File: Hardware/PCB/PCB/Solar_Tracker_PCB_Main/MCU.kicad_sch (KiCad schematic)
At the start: 1 part, among them IC1 ESP32-S3-WROOM-1-N4R8

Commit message: actualizacion de pcb
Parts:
- added C13: 22u, symbol Device:C
- added C16, C18, C19: 0.1u, symbol Device:C
- added C17: 1u, symbol Device:C
- added R16: 0, symbol Device:R
- added R2: 10k, symbol Device:R
- added SW1, SW3: ~, symbol Switch:SW_MEC_5G
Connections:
- net GND: now reaches IC1.1 (GND_1)
- net GND: now also IC1.40 (GND_2), IC1.41 (GND_3), IC1.42 (GND_4), IC1.43 (GND_5), IC1.44 (GND_6), IC1.45 (GND_7), IC1.46 (GND_8), IC1.47 (GND_9), IC1.48 (GND_10), IC1.49 (GND_11), C13.2, C16.2, C17.2, C18.2, C19.2, SW1.1 (A), SW1.2 (A), SW3.1 (A), SW3.2 (A)
- net VDD: now reaches IC1.2 (3V3)
- net VDD: now also C13.1, C16.1, R2.1
- net BOOT: now reaches IC1.27 (IO0)
- net BOOT: now also C19.1, SW3.3 (B), SW3.4 (B)
- net EN: now reaches IC1.3 (EN)
- net EN: now also C17.1, R16.2, R2.2
- new net: C18.1, R16.1, SW1.3 (B), SW1.4 (B)
- no-connect marks 0 -> 35
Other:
- moved on the sheet: IC1

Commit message: actualizacion pcb principal
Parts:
- removed R16: 0, symbol Device:R
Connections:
- net EN: now also C18.1, SW1.3 (B), SW1.4 (B)
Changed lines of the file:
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@@
-	(wire
-		(pts
-			(xy 96.52 22.86) (xy 97.79 22.86)
-		)
-		(stroke
-			(width 0)
-			(type default)
-		)
-	)
 	(wire
 		(pts
@@
 	(wire
 		(pts
-			(xy 86.36 22.86) (xy 88.9 22.86)
+			(xy 86.36 22.86) (xy 97.79 22.86)
 		)
 		(stroke
@@
 		(pts
 			(xy 71.12 22.86) (xy 71.12 29.21)
+		)
+		(stroke
+			(width 0)
+			(type default)
+		)
+	)
+	(wire
+		(pts
+			(xy 30.48 34.29) (xy 30.48 33.02)
 		)
 		(stroke
@@
 	(symbol
 		(lib_id "power:GND")
-		(at 30.48 33.02 0)
+		(at 30.48 34.29 0)
 		(unit 1)
 		(exclude_from_sim no)
@@
 		(fields_autoplaced yes)
 		(property "Reference" "#PWR042"
+			(at 30.48 40.64 0)
+			(effects
+				(font
+					(size 1.27 1.27)
+				)
+				(hide yes)
+			)
+		)
+		(property "Value" "GND"
 			(at 30.48 39.37 0)
 			(effects
@@
 					(size 1.27 1.27)
 				)
-				(hide yes)
-			)
-		)
-		(property "Value" "GND"
-			(at 30.48 38.1 0)
-			(effects
-				(font
-					(size 1.27 1.27)
-				)
 			)
 		)
 		(property "Footprint" ""
-			(at 30.48 33.02 0)
+			(at 30.48 34.29 0)
 			(effects
 				(font
@@
 		)
 		(property "Datasheet" ""
-			(at 30.48 33.02 0)
+			(at 30.48 34.29 0)
 			(effects
 				(font
@@
 		)
 		(property "Description" "Power symbol creates a global label with name \"GND\" , ground"
-			(at 30.48 33.02 0)
+			(at 30.48 34.29 0)
 			(effects
 				(font
@@
 					(unit 1)
 				)
-			)
-		)
-	)
-	(symbol
-		(lib_id "Device:R")
-		(at 92.71 22.86 90)
-		(unit 1)
-		(exclude_from_sim no)
-		(in_bom yes)
-		(on_board yes)
-		(dnp no)
-		(property "Reference" "R16"
-			(at 92.71 18.796 90)
-			(effects
-				(font
-					(size 1.27 1.27)
-				)
-			)
-		)
-		(property "Value" "0"
-			(at 92.71 20.574 90)
-			(effects
-				(font
-					(size 1.27 1.27)
-				)
-			)
-		)
-		(property "Footprint" ""
-			(at 92.71 24.638 90)
-			(effects
-				(font
-					(size 1.27 1.27)
-				)
-				(hide yes)
-			)
-		)
-		(property "Datasheet" "~"
-			(at 92.71 22.86 0)
-			(effects
-				(font
-					(size 1.27 1.27)
-				)
-				(hide yes)
-			)
-		)
-		(property "Description" "Resistor"
-			(at 92.71 22.86 0)
-			(effects
-				(font
-					(size 1.27 1.27)
-				)
-				(hide yes)
-			)
-		)
-		(pin "2"
-		)
-		(pin "1"
-		)
-		(instances
-			(project "Solar_Tracker_PCB_Main"
-				(path "/99b6ddd9-7ffe-4c85-972a-e0f594a166d4/521ed49f-67a8-4f65-9cb7-064f532bae28"
-					(reference "R16")
-					(unit 1)
-				)

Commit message: Actualizacion de Footprints Resistencias y Capacitores Main PCB
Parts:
- C13, C16, C17, C18, C19: footprint (none) -> Capacitor_SMD:C_0805_2012Metric_Pad1.18x1.45mm_HandSolder
- R2: footprint (none) -> Resistor_SMD:R_0805_2012Metric_Pad1.20x1.40mm_HandSolder
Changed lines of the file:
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@@
 			)
 		)
-		(property "Footprint" ""
+		(property "Footprint" "Capacitor_SMD:C_0805_2012Metric_Pad1.18x1.45mm_HandSolder"
 			(at 117.8052 35.56 0)
 			(effects
@@
 			)
 		)
-		(property "Footprint" ""
+		(property "Footprint" "Resistor_SMD:R_0805_2012Metric_Pad1.20x1.40mm_HandSolder"
 			(at 54.61 29.718 90)
 			(effects
@@
 			)
 		)
-		(property "Footprint" ""
+		(property "Footprint" "Capacitor_SMD:C_0805_2012Metric_Pad1.18x1.45mm_HandSolder"
 			(at 50.8 33.9852 0)
 			(effects
@@
 			)
 		)
-		(property "Footprint" ""
+		(property "Footprint" "Capacitor_SMD:C_0805_2012Metric_Pad1.18x1.45mm_HandSolder"
 			(at 74.93 30.1752 0)
 			(effects
@@
 			)
 		)
-		(property "Footprint" ""
+		(property "Footprint" "Capacitor_SMD:C_0805_2012Metric_Pad1.18x1.45mm_HandSolder"
 			(at 21.2852 33.02 0)
 			(effects
@@
 			)
 		)
-		(property "Footprint" ""
+		(property "Footprint" "Capacitor_SMD:C_0805_2012Metric_Pad1.18x1.45mm_HandSolder"
 			(at 31.4452 33.02 0)
 			(effects

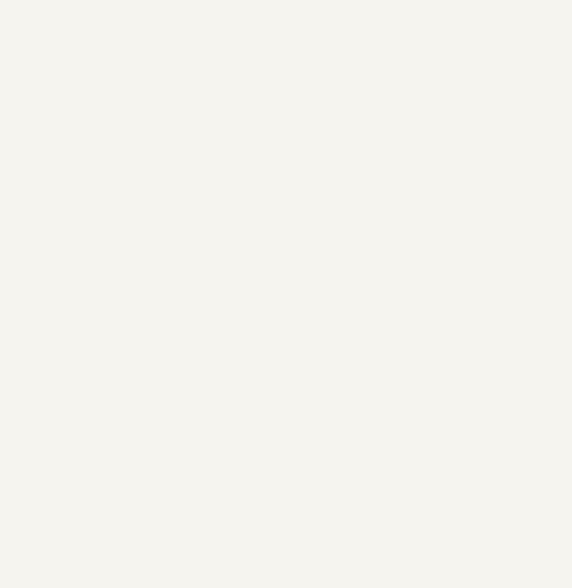
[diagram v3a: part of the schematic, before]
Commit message: Anhadir Footprint USBC
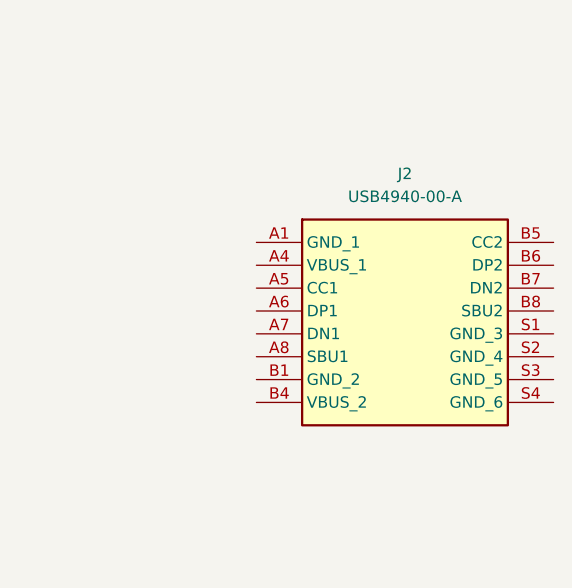
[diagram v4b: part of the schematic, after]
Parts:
- added J2: USB4940-00-A, USB4940:USB494000A, symbol USB4940-00-A:USB4940-00-A
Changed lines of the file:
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@@
+	)
+	(symbol
+		(lib_id "USB4940-00-A:USB4940-00-A")
+		(at 195.58 77.47 0)
+		(unit 1)
+		(exclude_from_sim no)
+		(in_bom yes)
+		(on_board yes)
+		(dnp no)
+		(fields_autoplaced yes)
+		(property "Reference" "J2"
+			(at 212.09 69.85 0)
+			(effects
+				(font
+					(size 1.27 1.27)
+				)
+			)
+		)
+		(property "Value" "USB4940-00-A"
+			(at 212.09 72.39 0)
+			(effects
+				(font
+					(size 1.27 1.27)
+				)
+			)
+		)
+		(property "Footprint" "USB4940:USB494000A"
+			(at 224.79 172.39 0)
+			(effects
+				(font
+					(size 1.27 1.27)
+				)
+				(justify left top)
+				(hide yes)
+			)
+		)
+		(property "Datasheet" "https://gct.co/download?type=PDFDrawing&name=USB4940.pdf"
+			(at 224.79 272.39 0)
+			(effects
+				(font
+					(size 1.27 1.27)
+				)
+				(justify left top)
+				(hide yes)
+			)
+		)
+		(property "Description" "USB-C (USB TYPE-C) USB 2.0 Receptacle Connector 24 (16+8 Dummy) Position Surface Mount, Right Angle , 48VDC , -40C ~ 85C"
+			(at 195.58 77.47 0)
+			(effects
+				(font
+					(size 1.27 1.27)
+				)
+				(hide yes)
+			)
+		)
+		(property "Height" "3.46"
+			(at 224.79 472.39 0)
+			(effects
+				(font
+					(size 1.27 1.27)
+				)
+				(justify left top)
+				(hide yes)
+			)
+		)
+		(property "Mouser Part Number" ""
+			(at 224.79 572.39 0)
+			(effects
+				(font
+					(size 1.27 1.27)
+				)
+				(justify left top)
+				(hide yes)
+			)
+		)
+		(property "Mouser Price/Stock" ""
+			(at 224.79 672.39 0)
+			(effects
+				(font
+					(size 1.27 1.27)
+				)
+				(justify left top)
+				(hide yes)
+			)
+		)
+		(property "Manufacturer_Name" "GCT (GLOBAL CONNECTOR TECHNOLOGY)"
+			(at 224.79 772.39 0)
+			(effects
+				(font
+					(size 1.27 1.27)
+				)
+				(justify left top)
+				(hide yes)
+			)
+		)
+		(property "Manufacturer_Part_Number" "USB4940-00-A"
+			(at 224.79 872.39 0)
+			(effects
+				(font
+					(size 1.27 1.27)
+				)
+				(justify left top)
+				(hide yes)
+			)
+		)
+		(pin "B6"
+		)
+		(pin "B8"
+		)
+		(pin "B5"
+		)
+		(pin "A6"
+		)
+		(pin "A8"
+		)
+		(pin "A4"
+		)
+		(pin "A1"
+		)
+		(pin "A5"
+		)
+		(pin "B1"
+		)
+		(pin "B4"
+		)
+		(pin "A7"
+		)
+		(pin "B7"
+		)
+		(pin "S3"
+		)
+		(pin "S1"
+		)
+		(pin "S2"
+		)
+		(pin "S4"
+		)
+		(instances
+			(project ""
+				(path "/99b6ddd9-7ffe-4c85-972a-e0f594a166d4/521ed49f-67a8-4f65-9cb7-064f532bae28"
+					(reference "J2")
+					(unit 1)
+				)
+			)
+		)
 	)
 	(symbol

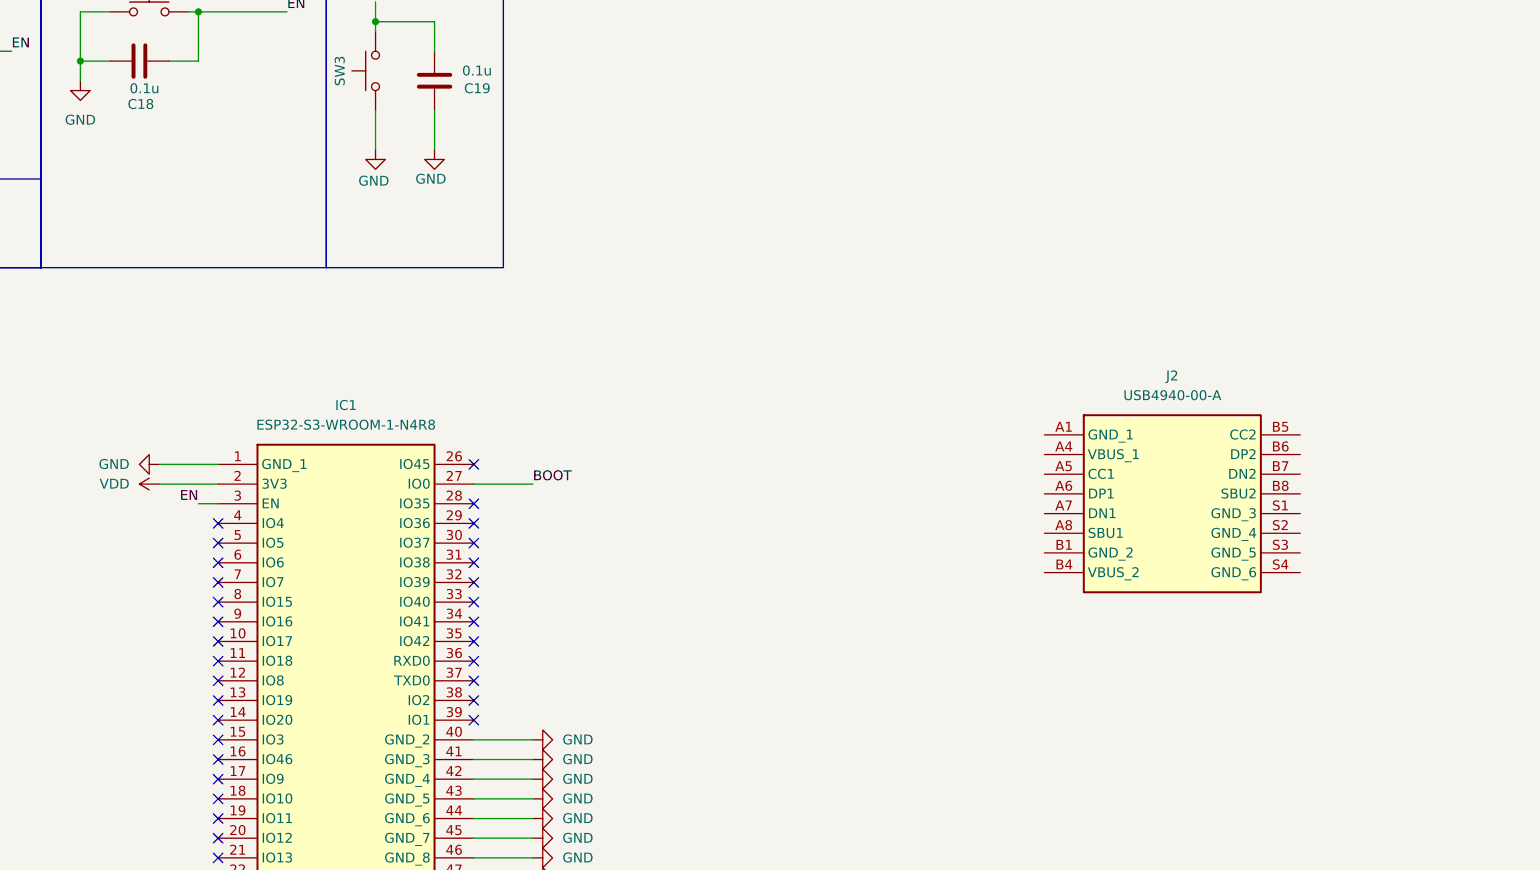
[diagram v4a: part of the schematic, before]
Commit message: Puerto USB con Regulador
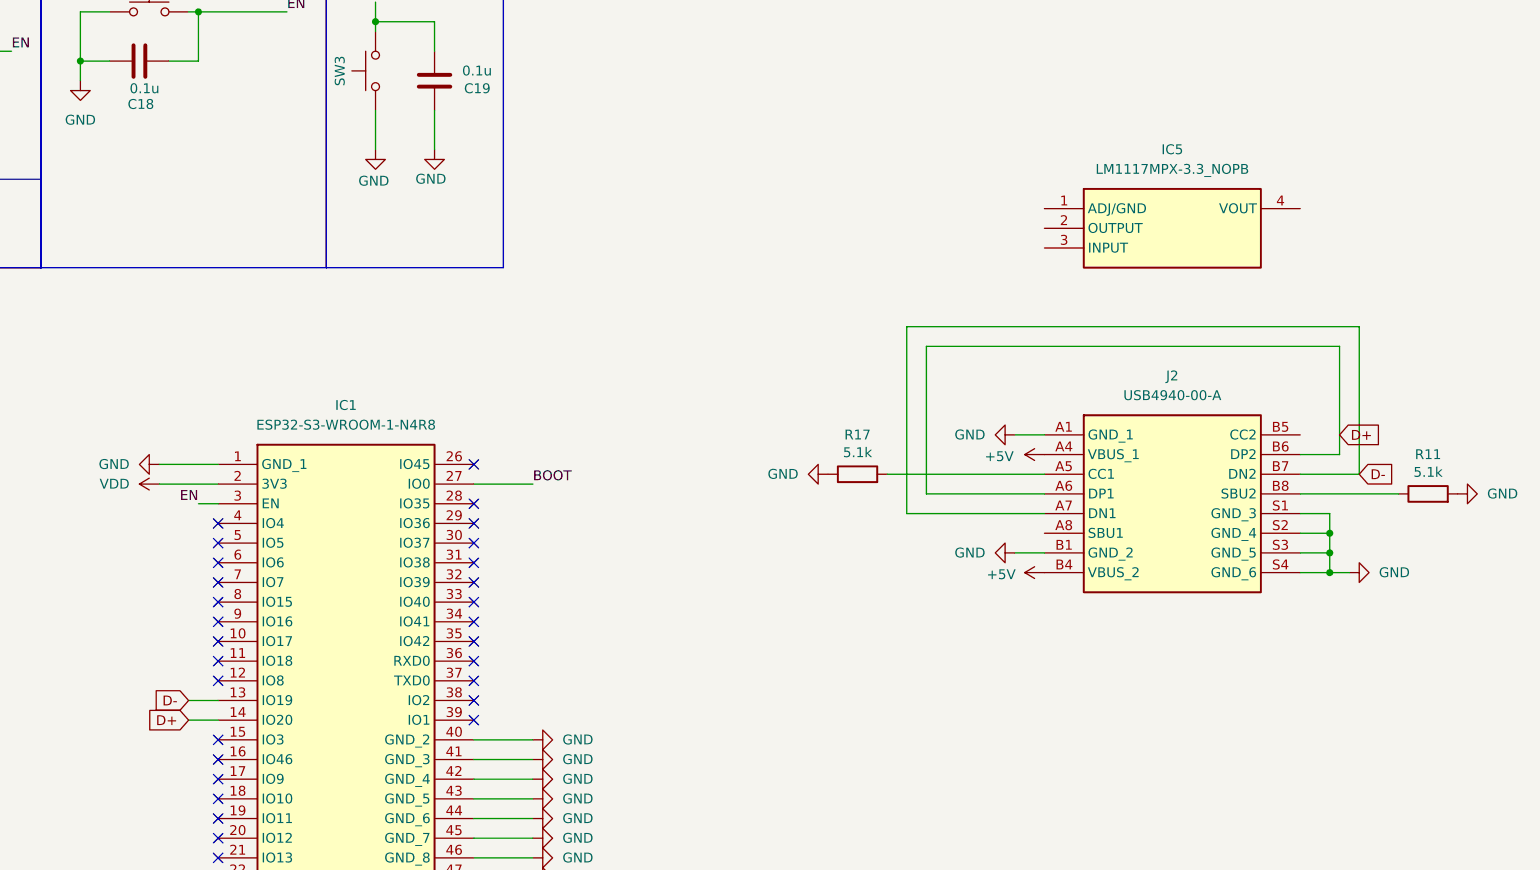
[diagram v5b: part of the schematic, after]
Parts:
- added IC5: LM1117MPX-3.3_NOPB, LM1117MPX3V3:SOT230P700X180-4N, symbol LM1117MPX-3_3_NOPB:LM1117MPX-3.3_NOPB
- added R11, R17: 5.1k, symbol Device:R
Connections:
- net GND: now also J2.A1 (GND_1), J2.B1 (GND_2), J2.S1 (GND_3), J2.S2 (GND_4), J2.S3 (GND_5), J2.S4 (GND_6), R11.2, R17.1
- net D-: now reaches IC1.13 (IO19)
- net D-: now also J2.A7 (DN1), J2.B7 (DN2)
- net D+: now reaches IC1.14 (IO20)
- net D+: now also J2.A6 (DP1), J2.B6 (DP2)
- net +5V: now reaches J2.A4 (VBUS_1)
- net +5V: now also J2.B4 (VBUS_2)
- net at J2.A5 (CC1): now also R17.2
- net at J2.B8 (SBU2): now also R11.1
- no-connect marks 35 -> 33

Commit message: Actualizacion Main pcb
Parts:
- removed R11: 5.1k, symbol Device:R
- removed SW1, SW3: ~, symbol Switch:SW_MEC_5G
- added C20: 10u, Capacitor_SMD:C_0805_2012Metric_Pad1.18x1.45mm_HandSolder, symbol Device:C_Polarized_Small_US
- added C21: 22u, Capacitor_SMD:C_0805_2012Metric_Pad1.18x1.45mm_HandSolder, symbol Device:C_Polarized_Small_US
- added J3: 1729076, 1729076:1729076, symbol 1729076:1729076
- added J4, J5: 1977223-1, 1977223:19772231, symbol 1977223-1:1977223-1
- added R18: 5.1k, Resistor_SMD:R_0805_2012Metric_Pad1.20x1.40mm_HandSolder, symbol Device:R
- R17: footprint (none) -> Resistor_SMD:R_0805_2012Metric_Pad1.20x1.40mm_HandSolder
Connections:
- net +5V: now also IC5.3 (INPUT), C20.1
- net BOOT: now also J5.1 (COM_1), J5.2 (COM_2)
- net EN: now also J4.1 (COM_1), J4.2 (COM_2)
- net GND: now also IC5.1 (ADJ/GND), C20.2, C21.2, J4.3 (NO_1), J4.4 (NO_2), J5.3 (NO_1), J5.4 (NO_2), R18.2
- net VDD: now also IC5.2 (OUTPUT), IC5.4 (VOUT), C21.1
- net RTC_SCL: now reaches IC1.24 (IO47)
- net RTC_SDA: now reaches IC1.25 (IO48)
- net IMU_INT: now reaches IC1.31 (IO38)
- net IMU_NRST: now reaches IC1.32 (IO39)
- net IMU_BOOTN: now reaches IC1.33 (IO40)
- net IMU_SDA: now reaches IC1.34 (IO41)
- net IMU_SCL: now reaches IC1.35 (IO42)
- net at J2.B5 (CC2): now also R18.1
- no-connect marks 33 -> 36
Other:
- note added: "Connect VOUT to the VDD plane for heat dissipation. Page 3"
- moved on the sheet: C18, C19, IC1, IC5, J2, R17
